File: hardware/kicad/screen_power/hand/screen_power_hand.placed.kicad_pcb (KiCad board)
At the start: 2 copper layers, 68 x 76 mm, 48 parts, among them J1 AUX 5V INPUT, J101 PI USB / XH4, J102 TOUCH / XH4, J103 SCREEN 1 POWER, J2 GPIO17 / GND, J201 PI USB / XH4, J202 TOUCH / XH4, J203 SCREEN 2 POWER, K101 IM02TS, K201 IM02TS, Q1 2N3904, Q101 TN0702, Q2 2N3906, Q201 TN0702, Q3 SUP70101EL, Q4 SUP70101EL, U1 LMC7660IN, U2 TLP627M

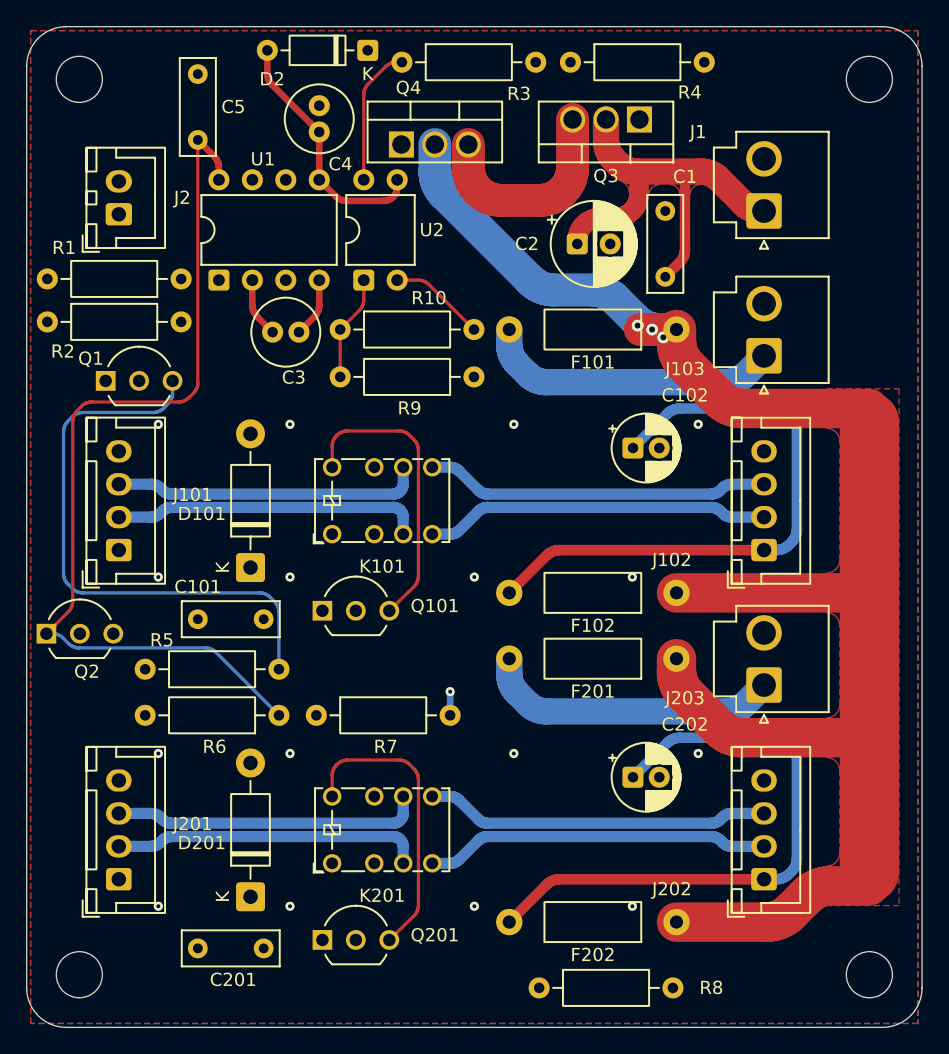
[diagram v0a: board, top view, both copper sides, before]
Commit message: fix(hardware): finish revision M USB routing and manufacturing package
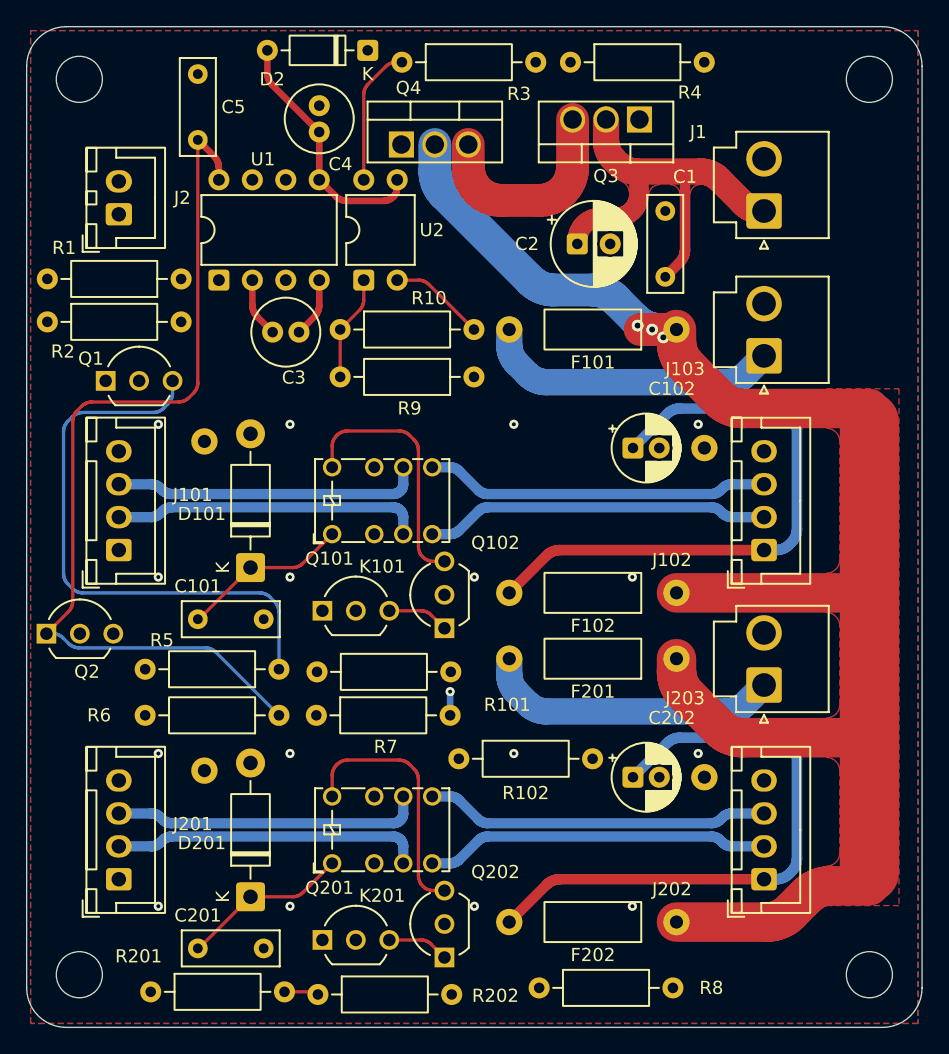
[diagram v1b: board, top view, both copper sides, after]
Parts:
- added Q102: TN0702, TO-92_Inline_Wide, F.Cu at (31.7, 45.7)
- added Q202: TN0702, TO-92_Inline_Wide, F.Cu at (31.7, 70.7)
- added R101: 10k 1%, R_Axial_DIN0207_L6.3mm_D2.5mm_P10.16mm_Horizontal, F.Cu at (22.1, 49.0)
- added R102: 100k 1%, R_Axial_DIN0207_L6.3mm_D2.5mm_P10.16mm_Horizontal, F.Cu at (32.8, 55.6)
- added R201: 10k 1%, R_Axial_DIN0207_L6.3mm_D2.5mm_P10.16mm_Horizontal, F.Cu at (9.42, 73.3)
- added R202: 100k 1%, R_Axial_DIN0207_L6.3mm_D2.5mm_P10.16mm_Horizontal, F.Cu at (22.1, 73.5)
- added TP101: SHIELD, TestPoint_THTPad_D2.0mm_Drill1.0mm, F.Cu at (13.5, 31.5)
- added TP102: SHIELD, TestPoint_THTPad_D2.0mm_Drill1.0mm, F.Cu at (51.5, 32.0)
- added TP201: SHIELD, TestPoint_THTPad_D2.0mm_Drill1.0mm, F.Cu at (13.5, 56.5)
- added TP202: SHIELD, TestPoint_THTPad_D2.0mm_Drill1.0mm, F.Cu at (51.5, 57.0)
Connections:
- C101 pad 1: HOST1_5V -> AUX_5V
- C201 pad 1: HOST2_5V -> AUX_5V
- D101 pad 1: HOST1_5V -> AUX_5V
- D201 pad 1: HOST2_5V -> AUX_5V
- K101 pad 1: HOST1_5V -> AUX_5V
- K201 pad 1: HOST2_5V -> AUX_5V
- Q101 pad 3: S1_DATA_COIL_LOW -> S1_RELAY_STACK
- Q201 pad 3: S2_DATA_COIL_LOW -> S2_RELAY_STACK
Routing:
- net AUX_5V: track 103.3 -> 129.0 mm
- net S2_RELAY_STACK: track 0.00 -> 4.69 mm
- net S1_RELAY_STACK: track 0.00 -> 4.69 mm
- net S2_DATA_COIL_LOW: track 22.7 -> 19.5 mm
- net S1_DATA_COIL_LOW: track 22.7 -> 19.5 mm
- net S2_HOST_PRESENT: track 0.00 -> 2.59 mm

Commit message: fix(hardware): close Claude PCB review findings
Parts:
- R2: value 100k 1% -> 4.7k 1%
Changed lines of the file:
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@@
 			)
 		)
-		(property "Value" "100k 1%"
+		(property "Value" "4.7k 1%"
 			(at 5.08 2.37 0)
 			(layer "F.Fab")

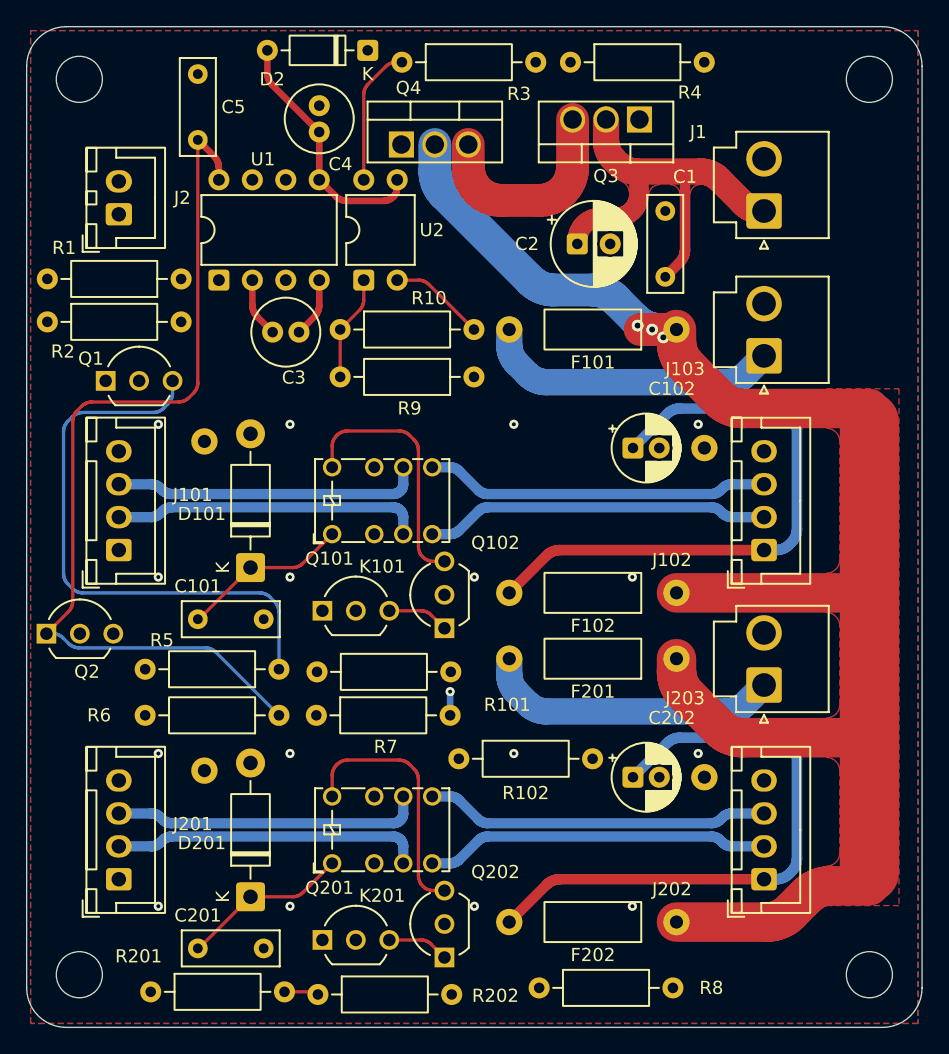
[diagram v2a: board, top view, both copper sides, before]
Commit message: feat(hardware): lower screen power cost and finish copper contours
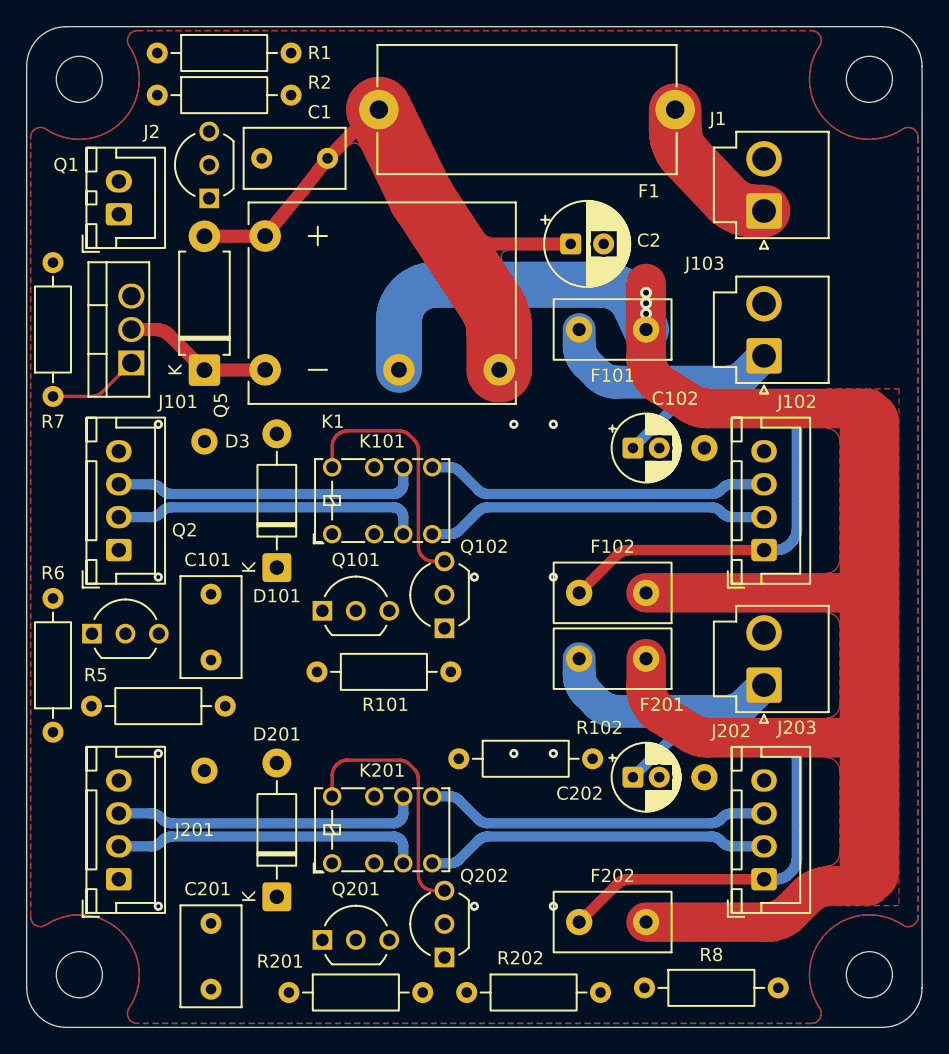
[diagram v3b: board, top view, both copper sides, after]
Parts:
- removed C3, C4: 10uF 25V bipolar, C_Radial_D5.0mm_H11.0mm_P2.00mm
- removed C5: 100nF 63V, C_Rect_L7.2mm_W2.5mm_P5.00mm
- removed D2: BAT85S, D_DO-35_SOD27_P7.62mm_Horizontal
- removed Q3, Q4: SUP70101EL, TO-220-3_SUP70101EL
- removed R10: 10k 1%, R_Axial_DIN0207_L6.3mm_D2.5mm_P10.16mm_Horizontal
- removed R3: 4.7k 1%, R_Axial_DIN0207_L6.3mm_D2.5mm_P10.16mm_Horizontal
- removed R4: 22k 1%, R_Axial_DIN0207_L6.3mm_D2.5mm_P10.16mm_Horizontal
- removed R9: 2.4k 1%, R_Axial_DIN0207_L6.3mm_D2.5mm_P10.16mm_Horizontal
- removed U1: LMC7660IN, DIP-8_W7.62mm
- removed U2: TLP627M, DIP-4_W7.62mm
- added D3: P6KE6.8CA, D_DO-15_P10.16mm_Horizontal, F.Cu at (13.5, 26.1)
- added F1: 8A time-lag, Fuseholder_Schurter_OGN_0031.8201, F.Cu at (49.2, 6.30)
- added K1: G6C-1117P-US, Relay_Omron_G6C-1117P-US, F.Cu at (18.1, 26.1)
- added Q5: IRLZ44N, TO-220-3_IRLZ44N, F.Cu at (7.95, 25.5)
- C1, C101, C201: value 100nF 63V -> 100nF 50V X7R; footprint C_Rect_L7.2mm_W2.5mm_P5.00mm -> C_Disc_D7.5mm_W4.4mm_P5.00mm
- F101, F201: value 4A fast -> 4A time-lag; footprint Fuse_Littelfuse_251_P12.70mm -> Fuse_Bel_0697H_P5.08mm
- F102, F202: value 750mA fast -> 800mA time-lag; footprint Fuse_Littelfuse_251_P12.70mm -> Fuse_Bel_0697H_P5.08mm
- R7: value 100k 1% -> 10k 1%
- moved R7 31.4 mm to (2.00, 28.1), turned to 90 degrees
- moved C1 27.2 mm to (22.9, 10.0), turned to 180 degrees
- moved R2 19.1 mm to (9.92, 5.20)
- moved R1 17.3 mm to (9.92, 2.00), turned to 0 degrees
- moved R6 17.2 mm to (2.00, 53.6), turned to 90 degrees
- moved Q1 15.9 mm to (13.9, 13.0), turned to 90 degrees
- moved R202 11.3 mm to (33.4, 73.3)
- moved R201 10.5 mm to (19.9, 73.3)
- moved R8 8.00 mm to (46.9, 73.0)
- moved R5 4.95 mm to (15.1, 51.6)
- moved Q2 3.46 mm to (4.96, 46.1)
- moved C101 3.26 mm to (14.0, 48.1), turned to 90 degrees
- moved C201 3.26 mm to (14.0, 73.1), turned to 90 degrees
- moved F101 2.31 mm to (47.0, 23.0)
- moved F102 2.31 mm to (47.0, 43.0)
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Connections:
- J1 pad 1: AUX_5V -> AUX_5V_IN
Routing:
- net AUX_5V: track 129.0 -> 48.5 mm
- net CONTROL_SINK: track 51.1 -> 0.00 mm
- net NEG_5V: track 19.1 -> 0.00 mm
- net COMMON_SOURCE: track 16.2 -> 0.00 mm
- net POWER_COIL_LOW: track 0.00 -> 11.4 mm
- net AUX_5V_IN: track 0.00 -> 11.3 mm
- net SWITCHED_5V: track 128.9 -> 140.2 mm
- net GATE_SINK: track 10.6 -> 0.00 mm
- net GATE_LED: track 8.04 -> 0.00 mm
- net DATA_ENABLE: track 0.00 -> 6.95 mm
- net S2_TOUCH_5V: track 46.1 -> 40.8 mm
- net S2_MAIN_5V: track 22.7 -> 17.4 mm
- net S1_TOUCH_5V: track 46.1 -> 40.8 mm
- net S1_MAIN_5V: track 22.7 -> 17.4 mm
- net S2_RELAY_STACK: track 4.69 -> 0.00 mm
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
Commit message: feat(hardware): carry USB shields through removable XH5 plugs
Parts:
- removed TP101, TP102, TP201, TP202: SHIELD, TestPoint_THTPad_D2.0mm_Drill1.0mm
- J101, J201: value PI USB / XH4 -> PI USB / XH5; footprint JST_XH_B4B-XH-A_1x04_P2.50mm_Vertical -> JST_XH_B5B-XH-A_1x05_P2.50mm_Vertical
- J102, J202: value TOUCH / XH4 -> TOUCH / XH5; footprint JST_XH_B4B-XH-A_1x04_P2.50mm_Vertical -> JST_XH_B5B-XH-A_1x05_P2.50mm_Vertical
- moved R5 13.0 mm to (28.1, 52.5)
- moved R7 8.50 mm to (2.00, 19.6)
- moved Q5 4.82 mm to (3.21, 24.6), turned to 0 degrees
- moved J103 1.40 mm to (56.0, 23.6)
- moved J203 0.77 mm to (56.0, 49.2)
- moved R6 0.70 mm to (2.00, 52.9)
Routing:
- net POWER_COIL_LOW: track 11.4 -> 19.1 mm
- net SWITCHED_5V: track 140.2 -> 137.6 mm
- net S1_TOUCH_5V: track 40.8 -> 42.5 mm
- net S2_TOUCH_5V: track 40.8 -> 42.5 mm
- net DATA_ENABLE: track 6.95 -> 5.52 mm
- net S2_MAIN_5V: track 17.4 -> 16.8 mm
